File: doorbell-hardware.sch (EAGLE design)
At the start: 14 parts, among them T1 BC846

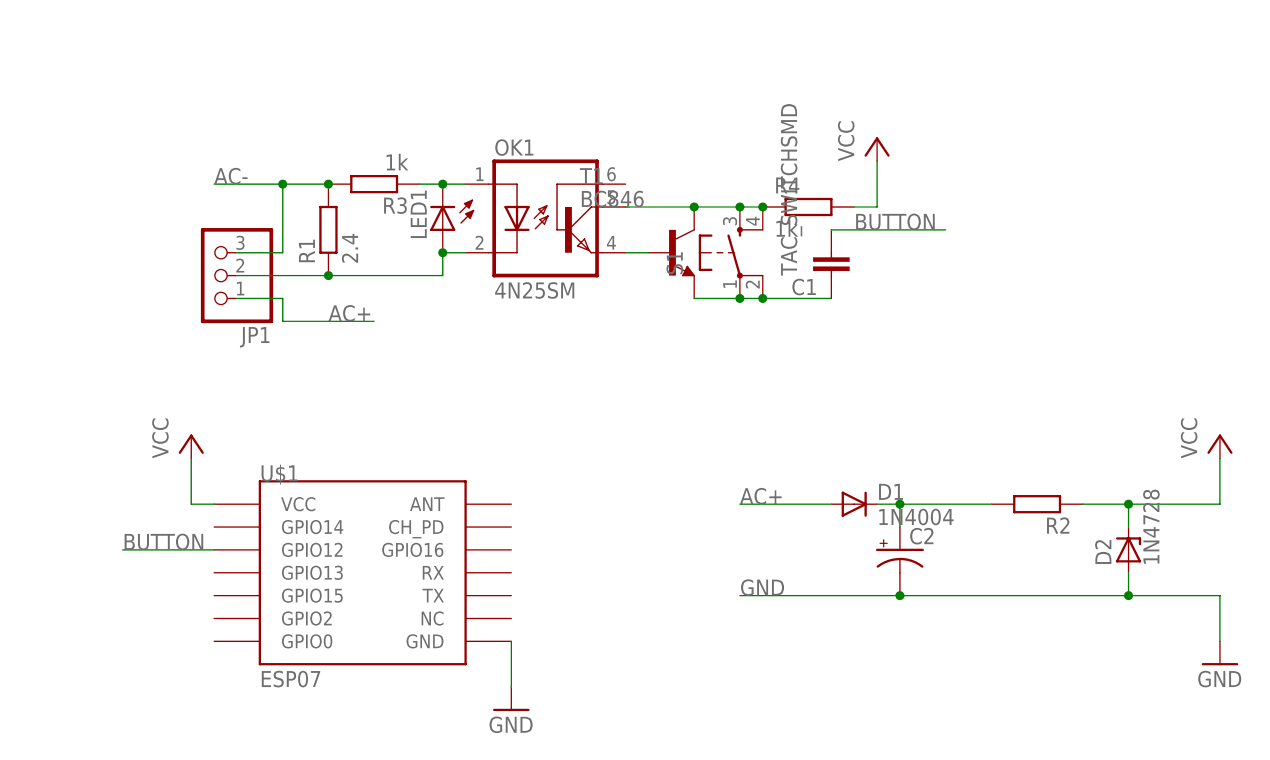
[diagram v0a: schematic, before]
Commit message: Replaced zener with ldo, started work on sleep and interrupt
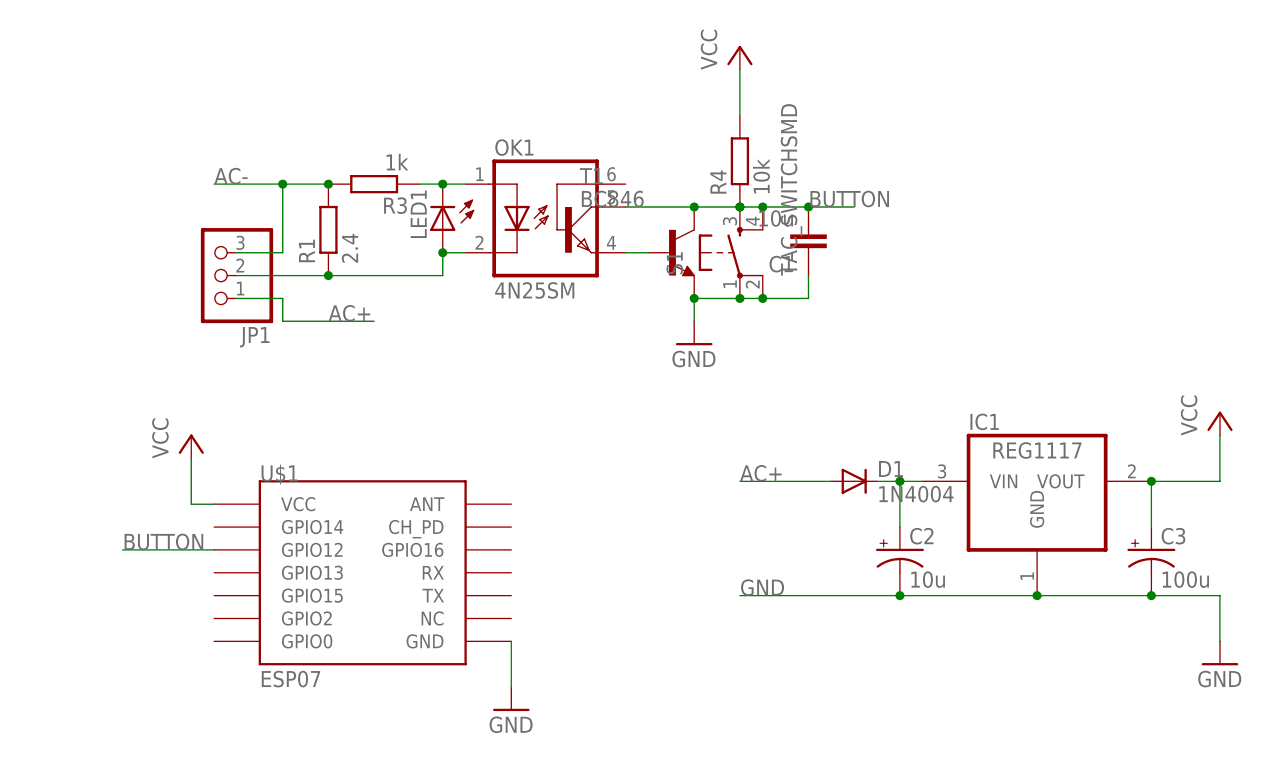
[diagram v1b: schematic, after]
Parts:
- removed D2: 1N4728, diode:1N4728
- removed R2: (no value), eagle-ltspice:R
- added C3: 100u, rcl:CPOL-USE2.5-5
- added IC1: REG1117, burr-brown:REG1117
- C1: value (none) -> 10u; device rcl:C-EUC1206 -> rcl:C-EU050-024X044
- C2: value (none) -> 10u
- R4: value 1k -> 10k
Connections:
- removed net N$5: OK1.COL, R4.1, S1.3, S1.4, T1.C
- removed net N$6: C1.1, S1.1, S1.2, T1.E
- net BUTTON: now also OK1.COL, R4.1, S1.3, S1.4, T1.C
- net GND: now also C1.1, C3.-, IC1.GND, S1.1, S1.2, T1.E; no longer D2.A
- net N$1: now also IC1.VIN; no longer R2.2
- net VCC: now also C3.+, IC1.VOUT; no longer D2.C, R2.1
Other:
- moved on the sheet: C1, D1, R4

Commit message: simplified circuit and code
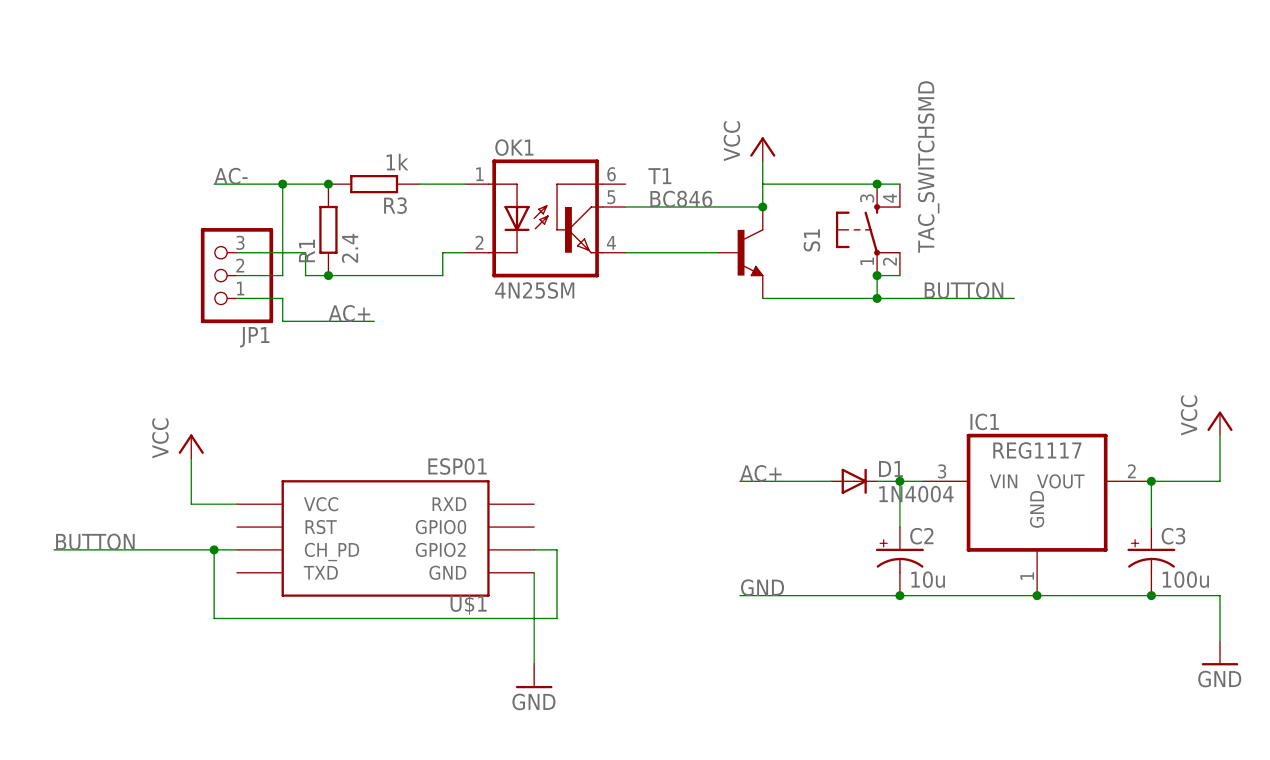
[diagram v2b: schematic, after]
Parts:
- removed C1: 10u, rcl:C-EU050-024X044
- removed LED1: (no value), adafruit:LED5MM
- removed R4: 10k, eagle-ltspice:R
- U$1: value ESP07 -> ESP01; device esp8266modules:ESP07 -> esp8266modules:ESP01
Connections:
- net AC-: now also JP1.2; no longer JP1.3
- net BUTTON: now also S1.1, S1.2, T1.E, U$1.CH_PD, U$1.GPIO2; no longer C1.2, OK1.COL, R4.1, S1.3, S1.4, T1.C, U$1.GPIO12
- net GND: no longer C1.1, S1.1, S1.2, T1.E
- net N$2: now also JP1.3; no longer JP1.2, LED1.A
- net N$3: no longer LED1.C
- net VCC: now also OK1.COL, S1.3, S1.4, T1.C; no longer R4.2
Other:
- moved on the sheet: S1, T1

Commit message: Working schematic and smaller layout
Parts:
- removed C3: 100u, rcl:CPOL-USE2.5-5
- removed IC1: REG1117, burr-brown:REG1117
- removed S1: TAC_SWITCHSMD, SparkFun-Electromechanical:TAC_SWITCHSMD
- added C1: 220u, resistor:CPOL-USE2-4
- added D2: 1N4148DO35-7, diode:1N4148DO35-7
- added JP2: (no value), pinhead:PINHD-1X2
- added R2: 1.2k, resistor:R-US_0204/5
- C2: value 10u -> 0.1u; device rcl:CPOL-USE2.5-5 -> capacitor-wima:C2.5/2
- D1: value 1N4004 -> BAT49; device diode:1N4004 -> diode:BAT49
- JP1: device pinhead:PINHD-1X3 -> pinhead:PINHD-1X2
- R1: value 2.4 -> 56k; device resistor:R-EU_0922_22 -> resistor:R-US_0204/5
- R3: value 1k -> 2.4; device eagle-ltspice:R -> resistor:R-US_0613/15
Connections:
- removed net AC+: D1.A, JP1.1
- removed net AC-: JP1.2, R1.2, R3.2
- new net N$6: C2.1, OK1.EMI, R2.2, T1.B
- new net N$9: D2.A, U$1.GPIO2
- net BUTTON: now also D2.C, R1.1; no longer S1.1, S1.2, T1.E, U$1.GPIO2
- net GND: now also C2.2, JP2.1, R2.1; no longer C2.-, C3.-, IC1.GND
- net N$1: now also D1.A, JP1.2, R3.2; no longer C2.+, D1.C, IC1.VIN
- net N$2: now also R1.2, T1.E; no longer JP1.3, OK1.C, R1.1
- net N$3: now also C1.+, D1.C; no longer R3.1
- net N$4: now also C1.-, JP1.1, OK1.C, R3.1; no longer OK1.EMI, T1.B
- net VCC: now also JP2.2; no longer C3.+, IC1.VOUT, S1.3, S1.4
